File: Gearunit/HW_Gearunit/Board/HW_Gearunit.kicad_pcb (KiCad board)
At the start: 4 copper layers, 27 x 32 mm, 86 parts, among them J1 XB-PJ-1837, J2 XB-PJ-1837, J3 Keystone 590, J4 TYPE-C-31-E-08, J5 Conn_01x05, J6 Keystone 590, Q2 DMC2400UV, Q3 DMC2400UV, Q4 AO3400A, Q5 AO3400A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

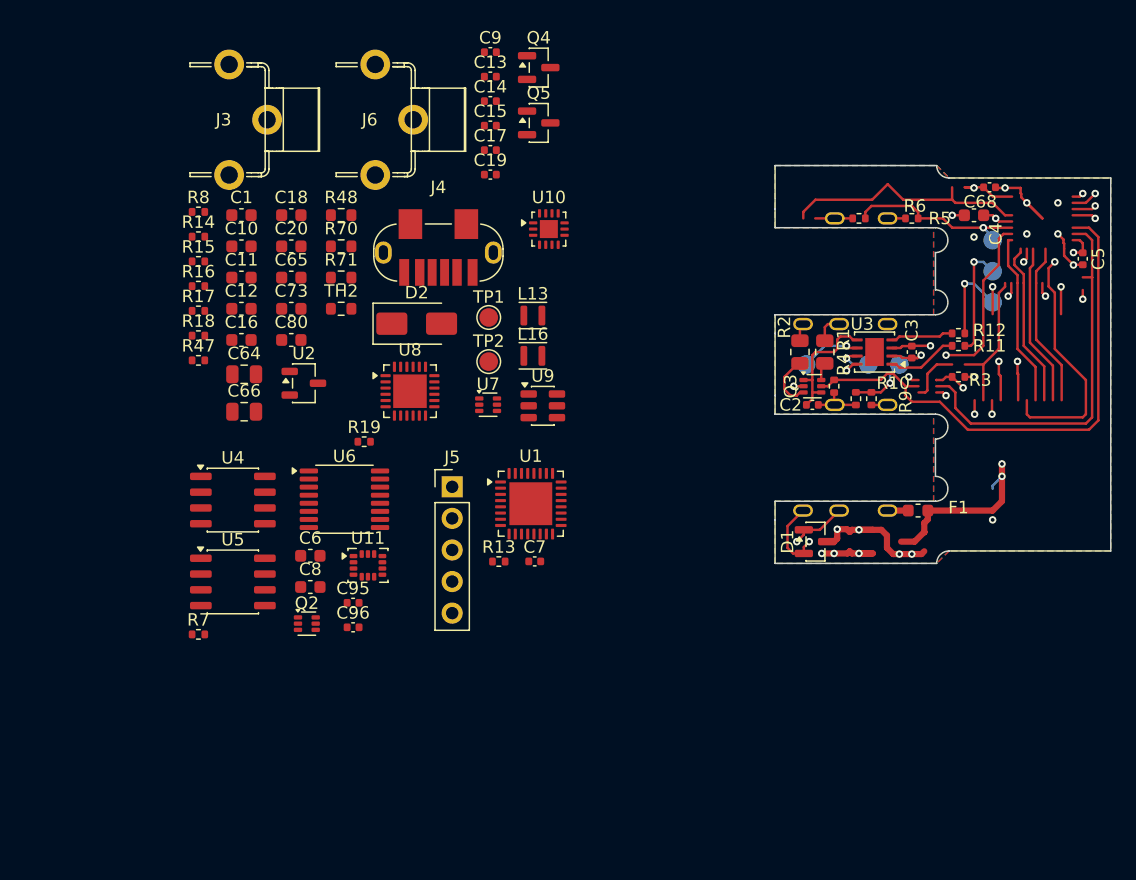
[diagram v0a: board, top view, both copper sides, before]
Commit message: Gearunit updates, Readme updated
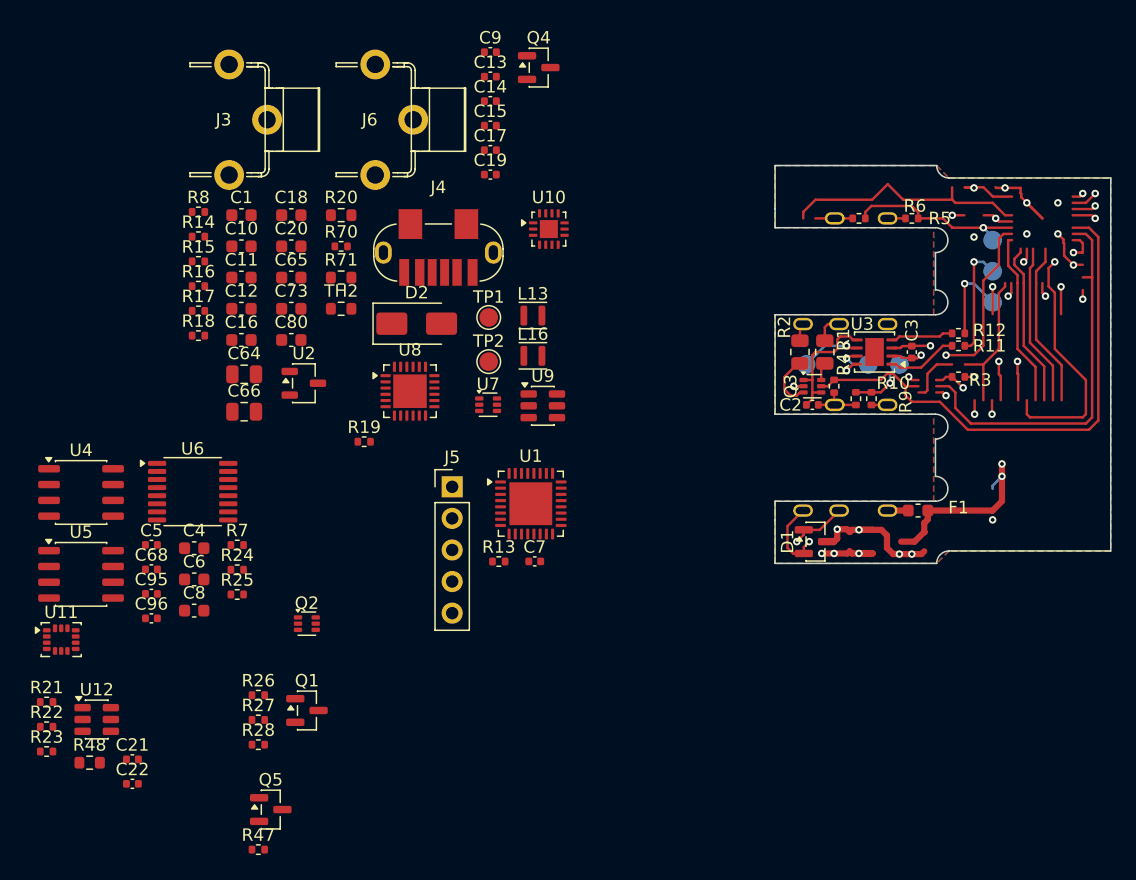
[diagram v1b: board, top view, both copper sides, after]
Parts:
- added C21: 100n, Capacitor_SMD:C_0402_1005Metric, F.Cu at (-51.7, 31.8)
- added C22: 100n, Capacitor_SMD:C_0402_1005Metric, F.Cu at (-51.7, 33.7)
- added Q1: AO3400A, Package_TO_SOT_SMD:SOT-23, F.Cu at (-37.7, 27.8)
- added R21: 10k, Resistor_SMD:R_0402_1005Metric, F.Cu at (-58.6, 27.1)
- added R22: 10k, Resistor_SMD:R_0402_1005Metric, F.Cu at (-58.6, 29.1)
- added R23: 10k, Resistor_SMD:R_0402_1005Metric, F.Cu at (-58.6, 31.1)
- added R24: 0R, Resistor_SMD:R_0402_1005Metric, F.Cu at (-43.3, 16.5)
- added R25: 0R, Resistor_SMD:R_0402_1005Metric, F.Cu at (-43.3, 18.5)
- added R26: 10k, Resistor_SMD:R_0402_1005Metric, F.Cu at (-41.6, 26.6)
- added R27: 15k, Resistor_SMD:R_0402_1005Metric, F.Cu at (-41.6, 28.6)
- added R28: 5.1k, Resistor_SMD:R_0402_1005Metric, F.Cu at (-41.6, 30.6)
- added R48: 30k, Resistor_SMD:R_0603_1608Metric, F.Cu at (-55.1, 32.0)
- added U12: INA181A1IDBV, Package_TO_SOT_SMD:SOT-23-6, F.Cu at (-54.6, 28.6)
- R20: renamed from R48; value 30k -> 100mR
- R70: footprint Resistor_SMD:R_0603_1608Metric -> Resistor_SMD:R_0402_1005Metric
- moved C5 78.4 mm to (-50.2, 14.5), turned to 0 degrees
- moved C68 74.1 mm to (-50.2, 16.5), turned to 0 degrees
- moved C4 68.2 mm to (-46.7, 14.8)
- moved Q5 59.3 mm to (-40.6, 35.8)
- moved R47 39.6 mm to (-41.6, 39.0)
- moved U11 25.4 mm to (-57.4, 22.1)
- moved C95 16.2 mm to (-50.2, 18.4)
- moved C96 16.2 mm to (-50.2, 20.4)
- moved U4 12.2 mm to (-55.8, 10.3)
- moved U5 12.2 mm to (-55.8, 16.9)
- moved U6 12.2 mm to (-46.8, 10.2)
- moved C6 9.53 mm to (-46.7, 17.3)
- moved C8 9.53 mm to (-46.7, 19.8)
- moved R7 7.84 mm to (-43.3, 14.5)
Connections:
- F1 pad 1: unconnected-(F1-Pad1) -> /PWR/VCAN
- J6 pad 1: /PWR/VBAT -> /MCU Sheet/BAT_V
- R18 pad 1: /PWR/USB_INT -> /MCU Sheet/USB_INT
- R20 pad 1: GND -> /MCU Sheet/BAT_V
- R20 pad 2: Net-(U8-TS) -> /PWR/VBAT
- R7 pad 1: /I2C_SEL -> /MCU Sheet/I2C_SEL
- R8 pad 2: /PWR/VBAT -> /MCU Sheet/BAT_V
- U1 pad 10: unconnected-(U1-PA4-Pad10) -> /MCU Sheet/BAT_I
- U1 pad 11: unconnected-(U1-PA5-Pad11) -> Net-(U1-PA5)
- U1 pad 14: unconnected-(U1-PB0-Pad14) -> /MCU Sheet/USB_INT
- U1 pad 15: unconnected-(U1-PB1-Pad15) -> /MCU Sheet/BAT_INT
- U1 pad 19: /MCU Sheet/CAN_TERM -> /MCU Sheet/CAN_RX
- U1 pad 20: unconnected-(U1-PA10-Pad20) -> Net-(Q1-G)
- U1 pad 26: unconnected-(U1-PB3-Pad26) -> /MCU Sheet/IMU_INT
- U10 pad 5: /PWR/USB_INT -> /MCU Sheet/USB_INT
- U10 pad 6: /PWR/I2C.SCL -> /MCU Sheet/I2C.SCL
- U10 pad 7: /PWR/I2C.SDA -> /MCU Sheet/I2C.SDA
- U11 pad 13: /I2C.SCL -> /MCU Sheet/I2C.SCL
- U11 pad 14: /I2C.SDA -> /MCU Sheet/I2C.SDA
- U11 pad 4: /IMU_INT -> /MCU Sheet/IMU_INT
- U4 pad 3: /POT_A -> Net-(U4-OUT)
- U5 pad 3: /POT_B -> Net-(U5-OUT)
- U6 pad 10: /I2C_SEL -> /MCU Sheet/I2C_SEL
- U6 pad 13: /I2C_SCL -> /MCU Sheet/I2C_SCL
- U6 pad 3: /I2C_SDA -> /MCU Sheet/I2C_SDA
- U8 pad 5: /PWR/I2C.SCL -> /MCU Sheet/I2C.SCL
- U8 pad 6: /PWR/I2C.SDA -> /MCU Sheet/I2C.SDA
- U8 pad 7: /PWR/BAT_INT -> /MCU Sheet/BAT_INT
